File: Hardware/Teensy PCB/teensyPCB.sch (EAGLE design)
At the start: 4 parts, among them U1 HC_05

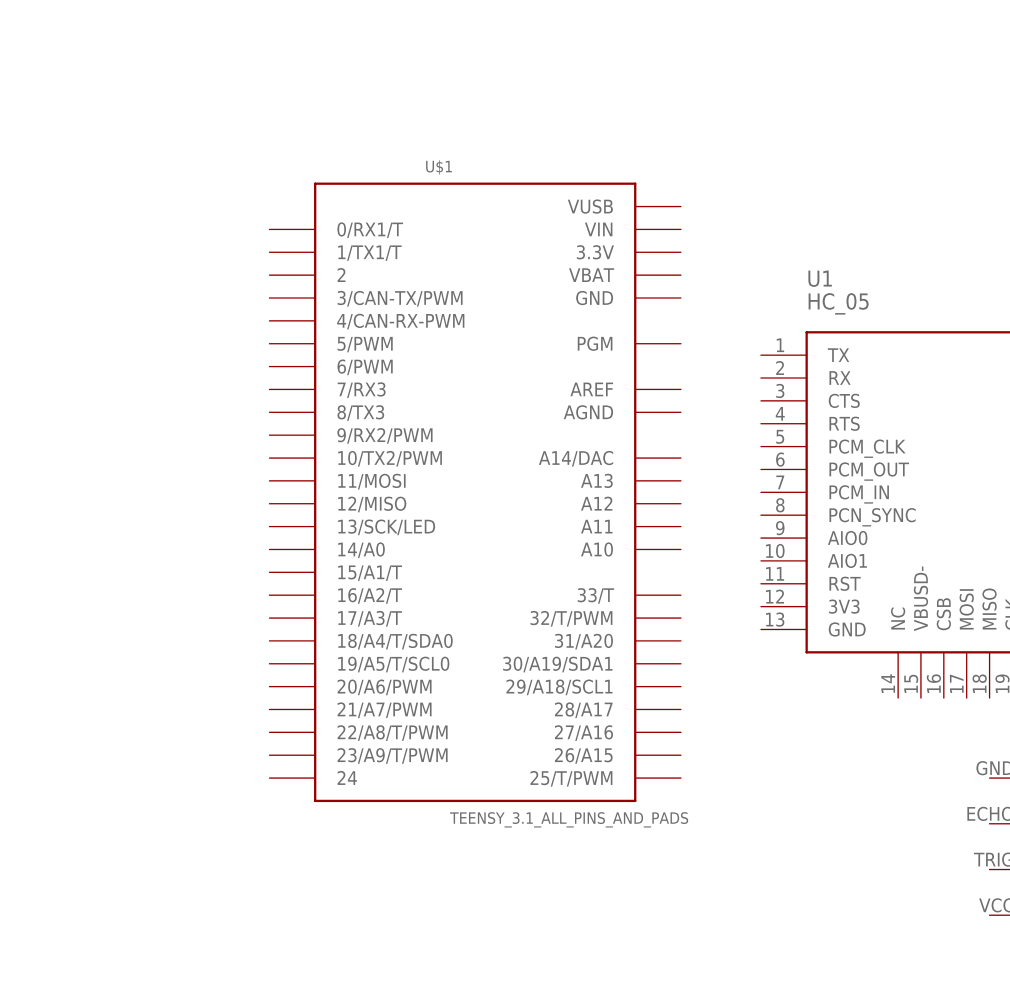
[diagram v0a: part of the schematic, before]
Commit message: reserving audio pins
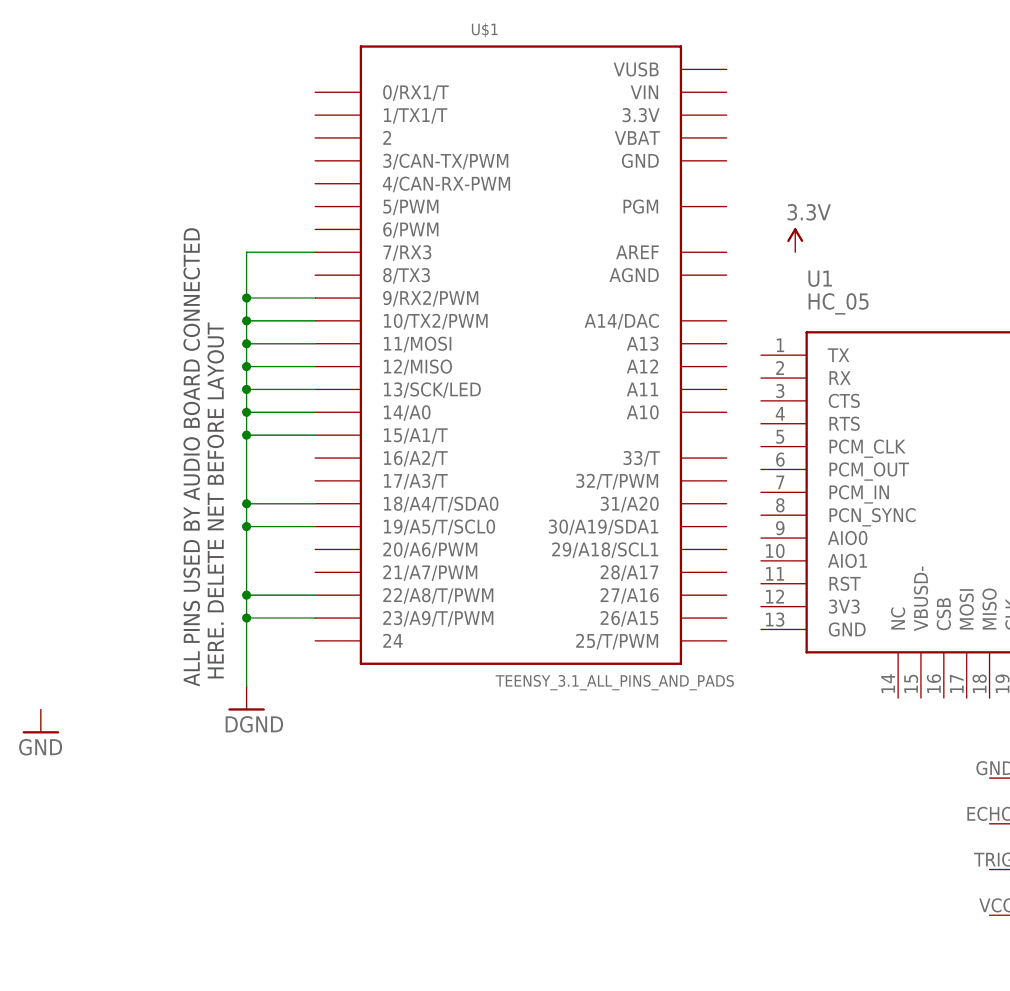
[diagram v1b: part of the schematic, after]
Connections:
- new net GND: U$1.10/TX2/PWM, U$1.11/MOSI, U$1.12/MISO, U$1.13/SCK/LED, U$1.14/A0, U$1.15/A1/T, U$1.18/A4/T/SDA0, U$1.19/A5/T/SCL0, U$1.22/A8/T/PWM, U$1.23/A9/T/PWM, U$1.7/RX3, U$1.9/RX2/PWM
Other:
- note added: "ALL PINS USED BY AUDIO BOARD CONNECTED HERE. DELETE NET BEFORE LAYOUT"
- moved on the sheet: U$1
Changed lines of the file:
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@@
 <layer number="101" name="Patch_Top" color="12" fill="4" visible="yes" active="yes"/>
 <layer number="102" name="Vscore" color="7" fill="1" visible="yes" active="yes"/>
+<layer number="103" name="tMap" color="7" fill="1" visible="yes" active="yes"/>
 <layer number="104" name="Name" color="7" fill="1" visible="yes" active="yes"/>
+<layer number="105" name="tPlate" color="7" fill="1" visible="yes" active="yes"/>
+<layer number="106" name="bPlate" color="7" fill="1" visible="yes" active="yes"/>
+<layer number="107" name="Crop" color="7" fill="1" visible="yes" active="yes"/>
+<layer number="108" name="tplace-old" color="10" fill="1" visible="no" active="yes"/>
+<layer number="109" name="ref-old" color="11" fill="1" visible="no" active="yes"/>
 <layer number="116" name="Patch_BOT" color="9" fill="4" visible="yes" active="yes"/>
 <layer number="121" name="_tsilk" color="7" fill="1" visible="yes" active="yes"/>
 <layer number="122" name="_bsilk" color="7" fill="1" visible="yes" active="yes"/>
+<layer number="125" name="_tNames" color="7" fill="1" visible="yes" active="yes"/>
+<layer number="144" name="Drill_legend" color="7" fill="1" visible="yes" active="yes"/>
 <layer number="151" name="HeatSink" color="7" fill="1" visible="yes" active="yes"/>
+<layer number="199" name="Contour" color="7" fill="1" visible="yes" active="yes"/>
 <layer number="200" name="200bmp" color="1" fill="10" visible="no" active="no"/>
 <layer number="201" name="201bmp" color="2" fill="1" visible="no" active="no"/>
 <layer number="202" name="202bmp" color="3" fill="1" visible="no" active="no"/>
+<layer number="203" name="203bmp" color="4" fill="10" visible="yes" active="yes"/>
+<layer number="204" name="204bmp" color="5" fill="10" visible="yes" active="yes"/>
+<layer number="205" name="205bmp" color="6" fill="10" visible="yes" active="yes"/>
+<layer number="206" name="206bmp" color="7" fill="10" visible="yes" active="yes"/>
+<layer number="207" name="207bmp" color="8" fill="10" visible="yes" active="yes"/>
+<layer number="208" name="208bmp" color="9" fill="10" visible="yes" active="yes"/>
+<layer number="209" name="209bmp" color="7" fill="1" visible="yes" active="yes"/>
+<layer number="210" name="210bmp" color="7" fill="1" visible="yes" active="yes"/>
+<layer number="211" name="211bmp" color="7" fill="1" visible="yes" active="yes"/>
+<layer number="212" name="212bmp" color="7" fill="1" visible="yes" active="yes"/>
+<layer number="213" name="213bmp" color="7" fill="1" visible="yes" active="yes"/>
+<layer number="214" name="214bmp" color="7" fill="1" visible="yes" active="yes"/>
+<layer number="215" name="215bmp" color="7" fill="1" visible="yes" active="yes"/>
+<layer number="216" name="216bmp" color="7" fill="1" visible="yes" active="yes"/>
+<layer number="217" name="217bmp" color="18" fill="1" visible="no" active="no"/>
+<layer number="218" name="218bmp" color="19" fill="1" visible="no" active="no"/>
+<layer number="219" name="219bmp" color="20" fill="1" visible="no" active="no"/>
+<layer number="220" name="220bmp" color="21" fill="1" visible="no" active="no"/>
+<layer number="221" name="221bmp" color="22" fill="1" visible="no" active="no"/>
+<layer number="222" name="222bmp" color="23" fill="1" visible="no" active="no"/>
+<layer number="223" name="223bmp" color="24" fill="1" visible="no" active="no"/>
+<layer number="224" name="224bmp" color="25" fill="1" visible="no" active="no"/>
 <layer number="250" name="Descript" color="3" fill="1" visible="no" active="no"/>
 <layer number="251" name="SMDround" color="12" fill="11" visible="no" active="no"/>
@@
 <part name="J_BT_BOARD_1" library="Bluetooth_HC-05" deviceset="BLUETOOTH_BOARD" device=""/>
 <part name="J_ULTRASONIC_1" library="HC-SR04" deviceset="HC-SR04" device=""/>
+<part name="SUPPLY1" library="SparkFun-Aesthetics" deviceset="3.3V" device=""/>
+<part name="GND1" library="SparkFun-Aesthetics" deviceset="GND" device=""/>
+<part name="GND2" library="SparkFun-Aesthetics" deviceset="DGND" device=""/>
 </parts>
 <sheets>
 <sheet>
 <plain>
+<text x="-27.94" y="-22.86" size="1.778" layer="97" rot="R90">ALL PINS USED BY AUDIO BOARD CONNECTED
+ HERE. DELETE NET BEFORE LAYOUT</text>
 </plain>
 <instances>
-<instance part="U$1" gate="G$1" x="0" y="0"/>
+<instance part="U$1" gate="G$1" x="5.08" y="15.24"/>
 <instance part="U1" gate="G$1" x="54.61" y="-1.27"/>
 <instance part="J_BT_BOARD_1" gate="J_BT_BOARD" x="110.49" y="-1.27" rot="R180"/>
 <instance part="J_ULTRASONIC_1" gate="J_ULTRASONIC" x="69.85" y="-40.64"/>
+<instance part="SUPPLY1" gate="G$1" x="35.56" y="25.4"/>
+<instance part="GND1" gate="1" x="-48.26" y="-27.94"/>
+<instance part="GND2" gate="G$1" x="-25.4" y="-25.4"/>
 </instances>
 <busses>
 </busses>
 <nets>
+<net name="GND" class="0">
+<segment>
+<pinref part="GND2" gate="G$1" pin="GND"/>
+<wire x1="-25.4" y1="-22.86" x2="-25.4" y2="-15.24" width="0.1524" layer="91"/>
+<pinref part="U$1" gate="G$1" pin="18/A4/T/SDA0"/>
+<wire x1="-25.4" y1="-15.24" x2="-25.4" y2="-12.7" width="0.1524" layer="91"/>
+<wire x1="-25.4" y1="-12.7" x2="-25.4" y2="-5.08" width="0.1524" layer="91"/>
+<wire x1="-25.4" y1="-5.08" x2="-25.4" y2="-2.54" width="0.1524" layer="91"/>
+<wire x1="-25.4" y1="-2.54" x2="-17.78" y2="-2.54" width="0.1524" layer="91"/>
+<pinref part="U$1" gate="G$1" pin="19/A5/T/SCL0"/>
+<wire x1="-17.78" y1="-5.08" x2="-25.4" y2="-5.08" width="0.1524" layer="91"/>
+<junction x="-25.4" y="-5.08"/>
+<pinref part="U$1" gate="G$1" pin="11/MOSI"/>
+<wire x1="-17.78" y1="15.24" x2="-25.4" y2="15.24" width="0.1524" layer="91"/>
+<wire x1="-25.4" y1="15.24" x2="-25.4" y2="12.7" width="0.1524" layer="91"/>
+<pinref part="U$1" gate="G$1" pin="9/RX2/PWM"/>
+<wire x1="-25.4" y1="12.7" x2="-25.4" y2="10.16" width="0.1524" layer="91"/>
+<wire x1="-25.4" y1="10.16" x2="-25.4" y2="7.62" width="0.1524" layer="91"/>
+<wire x1="-25.4" y1="7.62" x2="-25.4" y2="5.08" width="0.1524" layer="91"/>
+<wire x1="-25.4" y1="5.08" x2="-25.4" y2="-2.54" width="0.1524" layer="91"/>
+<wire x1="-17.78" y1="20.32" x2="-25.4" y2="20.32" width="0.1524" layer="91"/>
+<wire x1="-25.4" y1="20.32" x2="-25.4" y2="17.78" width="0.1524" layer="91"/>
+<pinref part="U$1" gate="G$1" pin="23/A9/T/PWM"/>
+<wire x1="-25.4" y1="17.78" x2="-25.4" y2="15.24" width="0.1524" layer="91"/>
+<wire x1="-17.78" y1="-15.24" x2="-25.4" y2="-15.24" width="0.1524" layer="91"/>
+<pinref part="U$1" gate="G$1" pin="22/A8/T/PWM"/>
+<wire x1="-17.78" y1="-12.7" x2="-25.4" y2="-12.7" width="0.1524" layer="91"/>
+<pinref part="U$1" gate="G$1" pin="13/SCK/LED"/>
+<wire x1="-17.78" y1="10.16" x2="-25.4" y2="10.16" width="0.1524" layer="91"/>
+<pinref part="U$1" gate="G$1" pin="15/A1/T"/>
+<wire x1="-17.78" y1="5.08" x2="-25.4" y2="5.08" width="0.1524" layer="91"/>
+<pinref part="U$1" gate="G$1" pin="12/MISO"/>
+<wire x1="-17.78" y1="12.7" x2="-25.4" y2="12.7" width="0.1524" layer="91"/>
+<pinref part="U$1" gate="G$1" pin="14/A0"/>
+<wire x1="-17.78" y1="7.62" x2="-25.4" y2="7.62" width="0.1524" layer="91"/>
+<pinref part="U$1" gate="G$1" pin="7/RX3"/>
+<wire x1="-17.78" y1="25.4" x2="-25.4" y2="25.4" width="0.1524" layer="91"/>
+<wire x1="-25.4" y1="25.4" x2="-25.4" y2="20.32" width="0.1524" layer="91"/>
+<pinref part="U$1" gate="G$1" pin="10/TX2/PWM"/>
+<wire x1="-17.78" y1="17.78" x2="-25.4" y2="17.78" width="0.1524" layer="91"/>
+<junction x="-25.4" y="-12.7"/>
+<junction x="-25.4" y="-15.24"/>
+<junction x="-25.4" y="5.08"/>
+<junction x="-25.4" y="7.62"/>
+<junction x="-25.4" y="10.16"/>
+<junction x="-25.4" y="12.7"/>
+<junction x="-25.4" y="15.24"/>
+<junction x="-25.4" y="17.78"/>
+<junction x="-25.4" y="20.32"/>
+<junction x="-25.4" y="-2.54"/>
+</segment>
+</net>
 </nets>
 </sheet>
@@
 </schematic>
 </drawing>
+<compatibility>
+<note version="6.3" minversion="6.2.2" severity="warning">
+Since Version 6.2.2 text objects can contain more than one line,
+which will not be processed correctly with this version.
+</note>
+</compatibility>
 </eagle>

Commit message: updates
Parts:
- added TOBALANCE: (no value), SparkFun-Connectors:M06POLAR_LOCK
- added U2: USD-SOCKETNEW, SparkFun-Connectors:USD-SOCKETNEW
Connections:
- new net 3.3V: TOBALANCE.5, U$1.3.3V
- new net 5V: TOBALANCE.6
- new net ARDUINO_RX: TOBALANCE.3
- new net ARDUINO_TX: TOBALANCE.2
- new net ENABLE: TOBALANCE.1
- net GND: now also TOBALANCE.4, U$1.GND; no longer U$1.10/TX2/PWM, U$1.11/MOSI, U$1.12/MISO, U$1.13/SCK/LED, U$1.14/A0, U$1.15/A1/T, U$1.18/A4/T/SDA0, U$1.19/A5/T/SCL0, U$1.22/A8/T/PWM, U$1.23/A9/T/PWM, U$1.7/RX3, U$1.9/RX2/PWM
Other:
- note removed: "ALL PINS USED BY AUDIO BOARD CONNECTED HERE. DELETE NET BEFORE LAYOUT"
- moved on the sheet: J_ULTRASONIC_1, U1

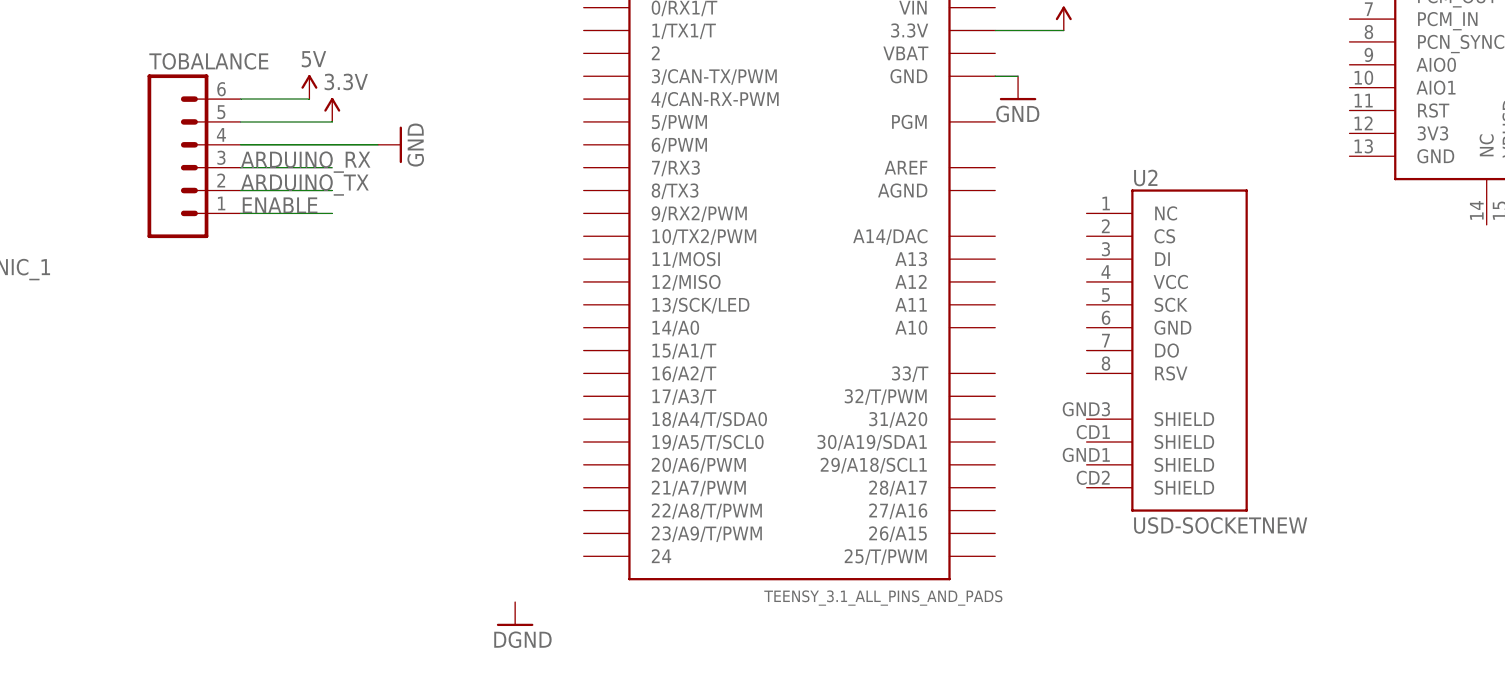
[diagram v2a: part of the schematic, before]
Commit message: Jeysen connected SD card in eagle schematic
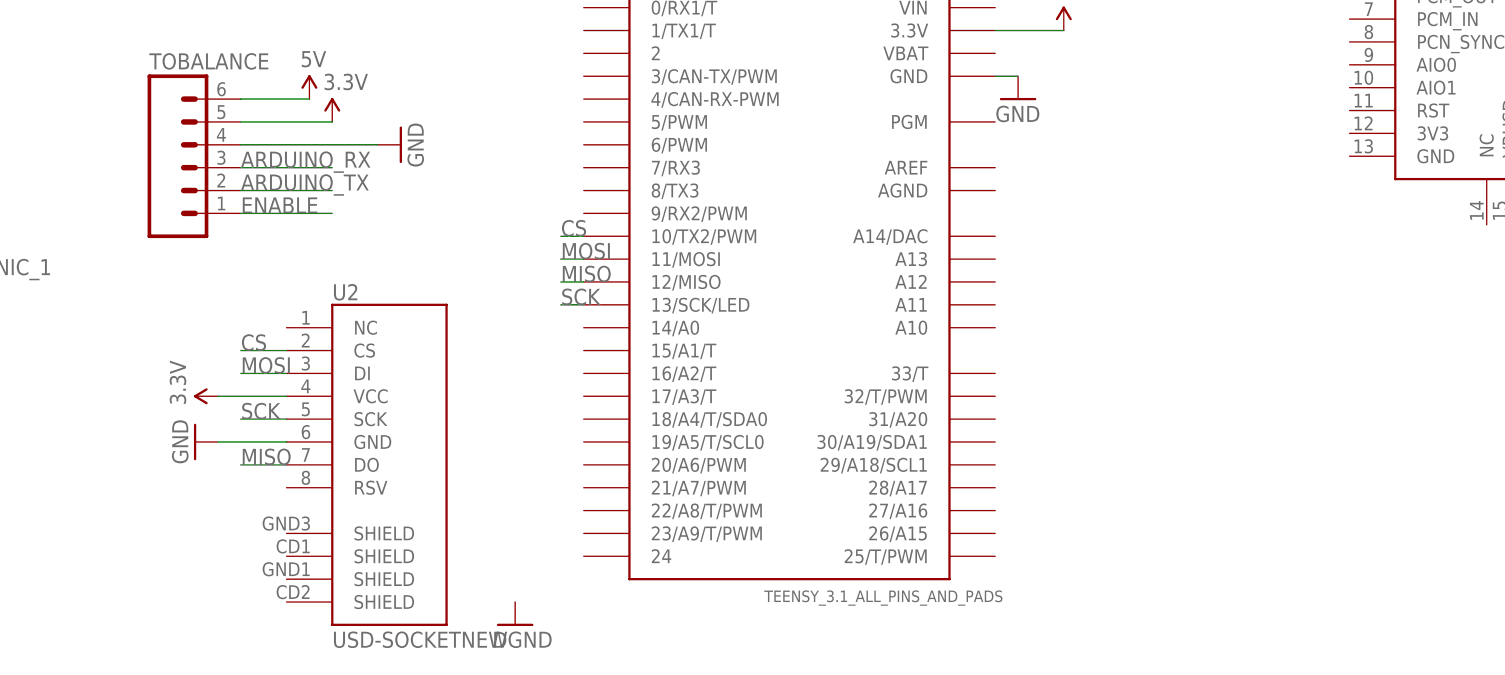
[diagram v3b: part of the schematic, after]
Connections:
- new net CS: U$1.10/TX2/PWM, U2.CS
- new net MISO: U$1.12/MISO, U2.DO
- new net MOSI: U$1.11/MOSI, U2.DI
- new net SCK: U$1.13/SCK/LED, U2.SCK
- net 3.3V: now also U2.VCC
- net GND: now also U2.GND
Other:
- moved on the sheet: U2
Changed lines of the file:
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@@
 <?xml version="1.0" encoding="utf-8"?>
 <!DOCTYPE eagle SYSTEM "eagle.dtd">
-<eagle version="7.2.0">
+<eagle version="7.5.0">
 <drawing>
 <settings>
@@
 <part name="SUPPLY3" library="SparkFun-Aesthetics" deviceset="3.3V" device=""/>
 <part name="GND3" library="SparkFun-Aesthetics" deviceset="GND" device=""/>
+<part name="GND4" library="SparkFun-Aesthetics" deviceset="GND" device=""/>
+<part name="SUPPLY4" library="SparkFun-Aesthetics" deviceset="3.3V" device=""/>
 </parts>
 <sheets>
@@
 <instance part="GND1" gate="1" x="30.48" y="33.02"/>
 <instance part="GND2" gate="G$1" x="-25.4" y="-25.4"/>
-<instance part="U2" gate="G$1" x="45.72" y="7.62"/>
+<instance part="U2" gate="G$1" x="-43.18" y="-5.08"/>
 <instance part="TOBALANCE" gate="G$1" x="-60.96" y="25.4"/>
 <instance part="SUPPLY2" gate="G$1" x="-48.26" y="33.02"/>
 <instance part="SUPPLY3" gate="G$1" x="-45.72" y="30.48"/>
 <instance part="GND3" gate="1" x="-38.1" y="27.94" rot="R90"/>
+<instance part="GND4" gate="1" x="-60.96" y="-5.08" rot="R270"/>
+<instance part="SUPPLY4" gate="G$1" x="-58.42" y="0" rot="R90"/>
 </instances>
 <busses>
@@
 <wire x1="-40.64" y1="27.94" x2="-55.88" y2="27.94" width="0.1524" layer="91"/>
 </segment>
+<segment>
+<pinref part="U2" gate="G$1" pin="GND"/>
+<pinref part="GND4" gate="1" pin="GND"/>
+<wire x1="-50.8" y1="-5.08" x2="-58.42" y2="-5.08" width="0.1524" layer="91"/>
+</segment>
 </net>
 <net name="3.3V" class="0">
@@
 <wire x1="-45.72" y1="30.48" x2="-55.88" y2="30.48" width="0.1524" layer="91"/>
 </segment>
+<segment>
+<pinref part="U2" gate="G$1" pin="VCC"/>
+<pinref part="SUPPLY4" gate="G$1" pin="3.3V"/>
+<wire x1="-50.8" y1="0" x2="-58.42" y2="0" width="0.1524" layer="91"/>
+</segment>
 </net>
 <net name="5V" class="0">
@@
 </segment>
 </net>
+<net name="SCK" class="0">
+<segment>
+<pinref part="U2" gate="G$1" pin="SCK"/>
+<wire x1="-50.8" y1="-2.54" x2="-55.88" y2="-2.54" width="0.1524" layer="91"/>
+<label x="-55.88" y="-2.54" size="1.778" layer="95"/>
+</segment>
+<segment>
+<pinref part="U$1" gate="G$1" pin="13/SCK/LED"/>
+<wire x1="-17.78" y1="10.16" x2="-20.32" y2="10.16" width="0.1524" layer="91"/>
+<label x="-20.32" y="10.16" size="1.778" layer="95"/>
+</segment>
+</net>
+<net name="MISO" class="0">
+<segment>
+<pinref part="U2" gate="G$1" pin="DO"/>
+<wire x1="-50.8" y1="-7.62" x2="-55.88" y2="-7.62" width="0.1524" layer="91"/>
+<label x="-55.88" y="-7.62" size="1.778" layer="95"/>
+</segment>
+<segment>
+<pinref part="U$1" gate="G$1" pin="12/MISO"/>
+<wire x1="-17.78" y1="12.7" x2="-20.32" y2="12.7" width="0.1524" layer="91"/>
+<label x="-20.32" y="12.7" size="1.778" layer="95"/>
+</segment>
+</net>
+<net name="MOSI" class="0">
+<segment>
+<pinref part="U2" gate="G$1" pin="DI"/>
+<wire x1="-50.8" y1="2.54" x2="-55.88" y2="2.54" width="0.1524" layer="91"/>
+<label x="-55.88" y="2.54" size="1.778" layer="95"/>
+</segment>
+<segment>
+<pinref part="U$1" gate="G$1" pin="11/MOSI"/>
+<wire x1="-17.78" y1="15.24" x2="-20.32" y2="15.24" width="0.1524" layer="91"/>
+<label x="-20.32" y="15.24" size="1.778" layer="95"/>
+</segment>
+</net>
+<net name="CS" class="0">
+<segment>
+<pinref part="U$1" gate="G$1" pin="10/TX2/PWM"/>
+<wire x1="-17.78" y1="17.78" x2="-20.32" y2="17.78" width="0.1524" layer="91"/>
+<label x="-20.32" y="17.78" size="1.778" layer="95"/>
+</segment>
+<segment>
+<pinref part="U2" gate="G$1" pin="CS"/>
+<wire x1="-50.8" y1="5.08" x2="-55.88" y2="5.08" width="0.1524" layer="91"/>
+<label x="-55.88" y="5.08" size="1.778" layer="95"/>
+</segment>
+</net>
